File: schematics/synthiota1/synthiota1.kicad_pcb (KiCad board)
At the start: 2 copper layers, 177.8 x 114.3 mm, 113 parts, among them J1 PJ-320A-4P DIP, J2 PJ-320A-4P DIP, SW1 RotaryEncoder_Switch_MP, U1 H11L1, U2 74HC4051, U3 MPR121QR2, U4 MPR121QR2

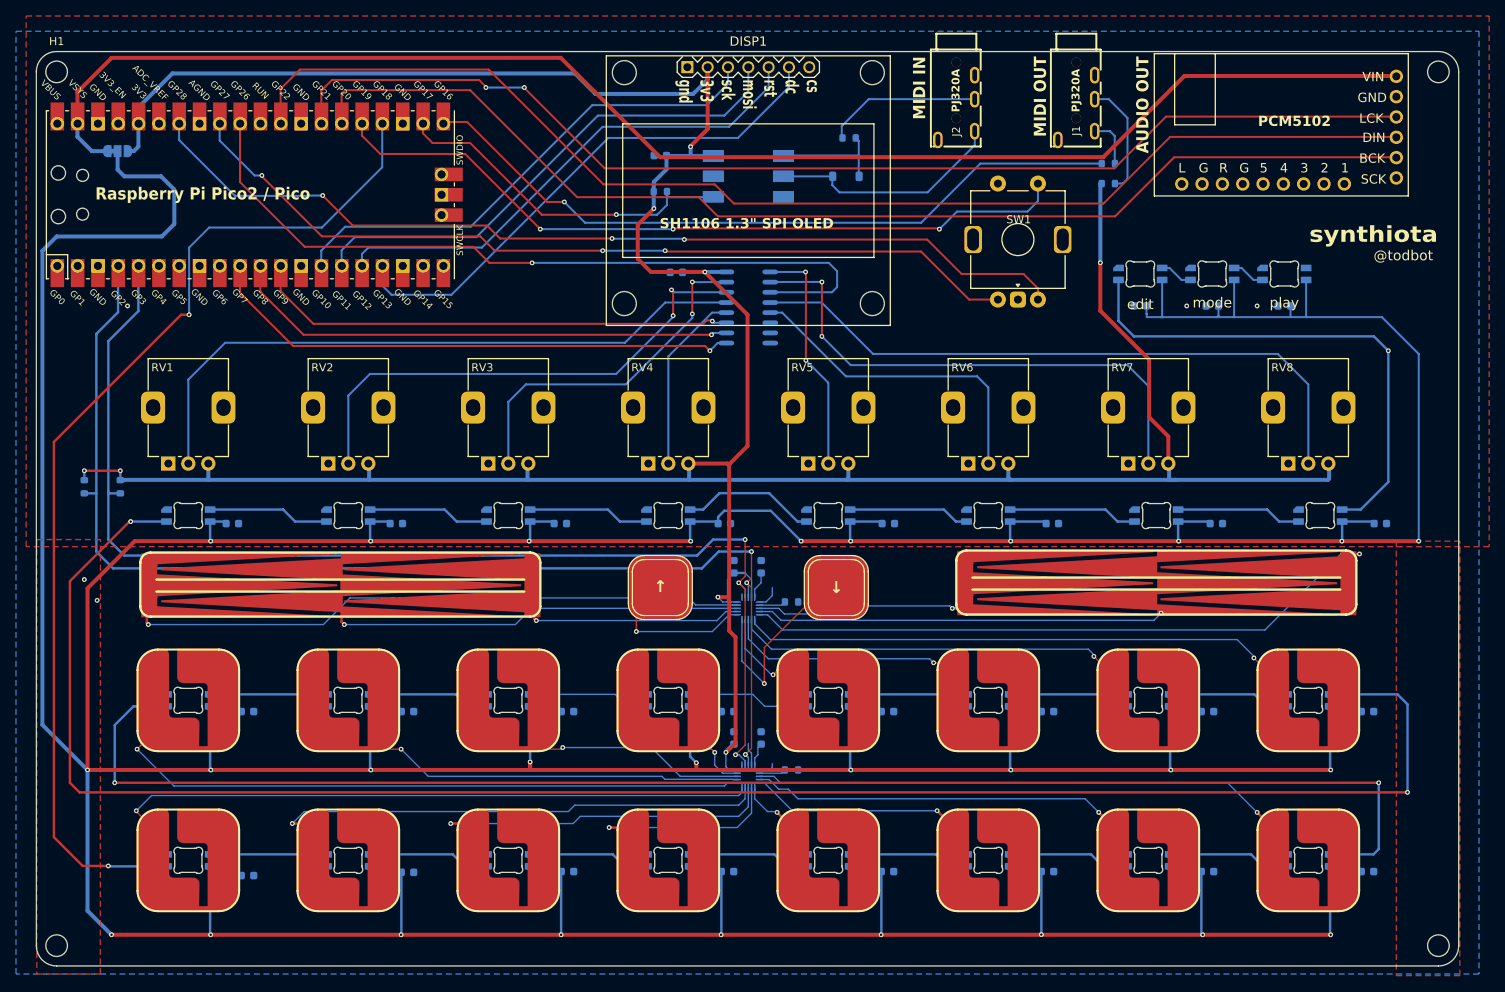
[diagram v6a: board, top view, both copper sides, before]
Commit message: moved pico numbers to back haha
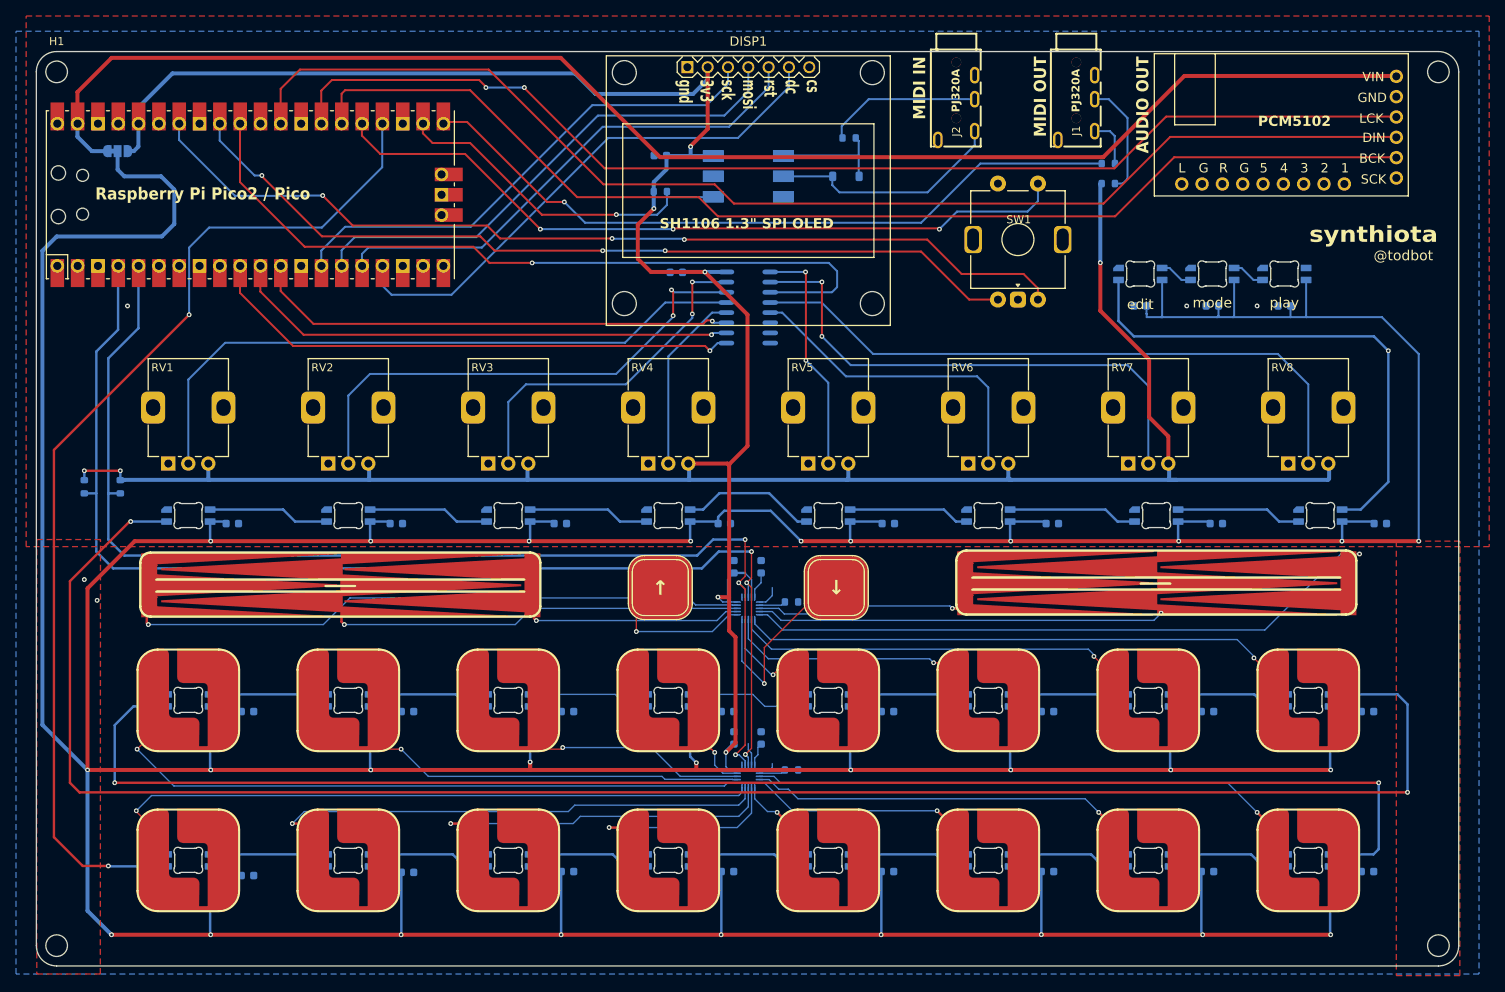
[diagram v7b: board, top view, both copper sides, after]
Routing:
- net /LEDDAT: track 130.8 -> 130.2 mm
